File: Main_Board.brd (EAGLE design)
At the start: 160.3 x 95.4 mm, 227 parts, among them J1 SERVO, J2 5.5x2.1mm Barrel, J3 9.7uH, J4 BATTERY, J5 SPEAKER, J6 SDIO-SDCARD, J7 header, P1 MOTOR_HEADER, P2 MOTOR_HEADER, P3 JTAG, Q1 SI9933CDY-PFET, Q2 CSD17308Q3, Q3 CSD17308Q3, Q4 CSD17308Q3, Q5 CSD17308Q3, Q6 CSD17308Q3, Q7 CSD17308Q3, Q8 CSD17308Q3, U1 LMS8117, U10 IMU, U11 LTC3122-MSOP, U12 CBAT54S-SOT23-3, U13 BQ2947, U14 TPA2005D1DGN, U15 BQ40Z60, U2 5V_BUCK_REG, U3 BTM7752G, U4 BTM7752G, U5 SN74LV4T125, U6 SN74LV4T125, U7 STM32F405RGT6, U8 RN4020RN4020, U9 BQ51013B-20VQFN

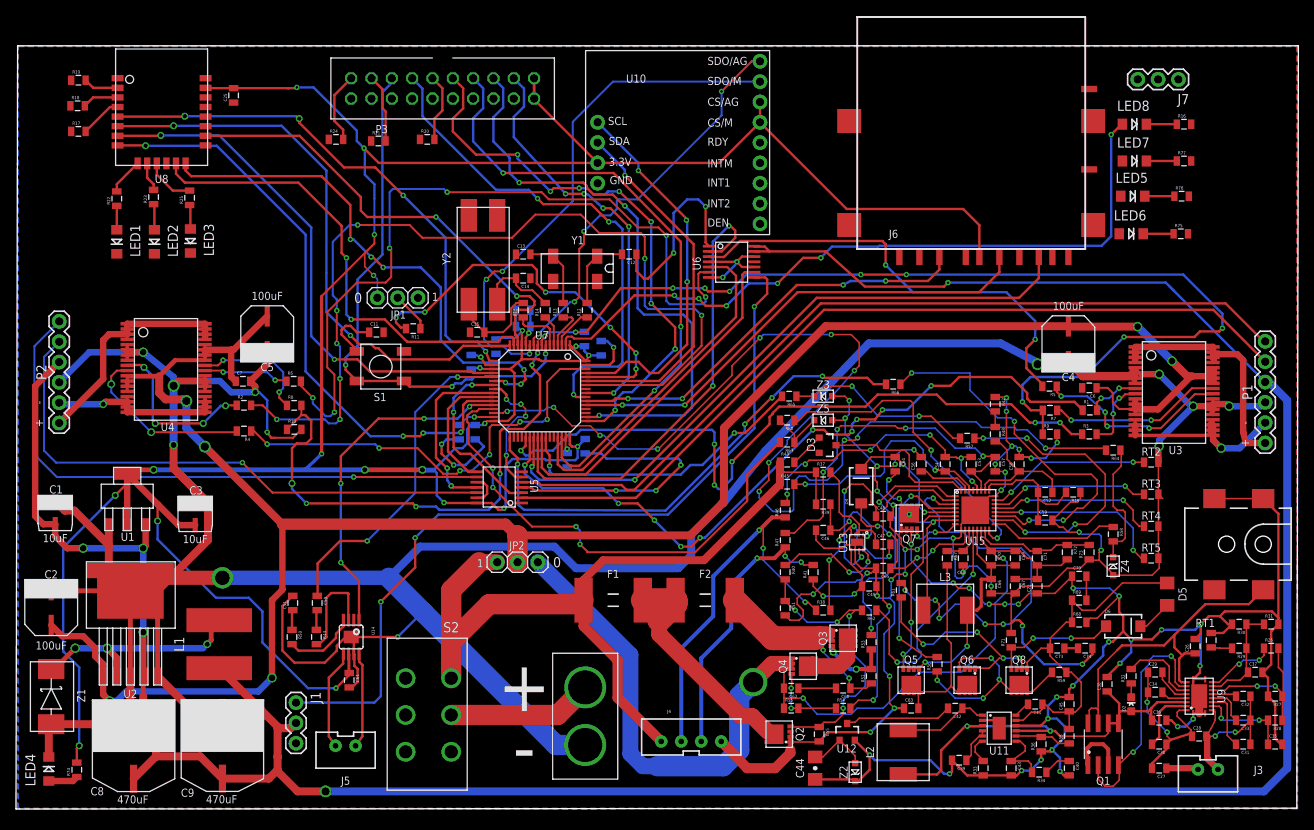
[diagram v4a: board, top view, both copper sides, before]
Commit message: routed LED, added standoffs, and refined routes
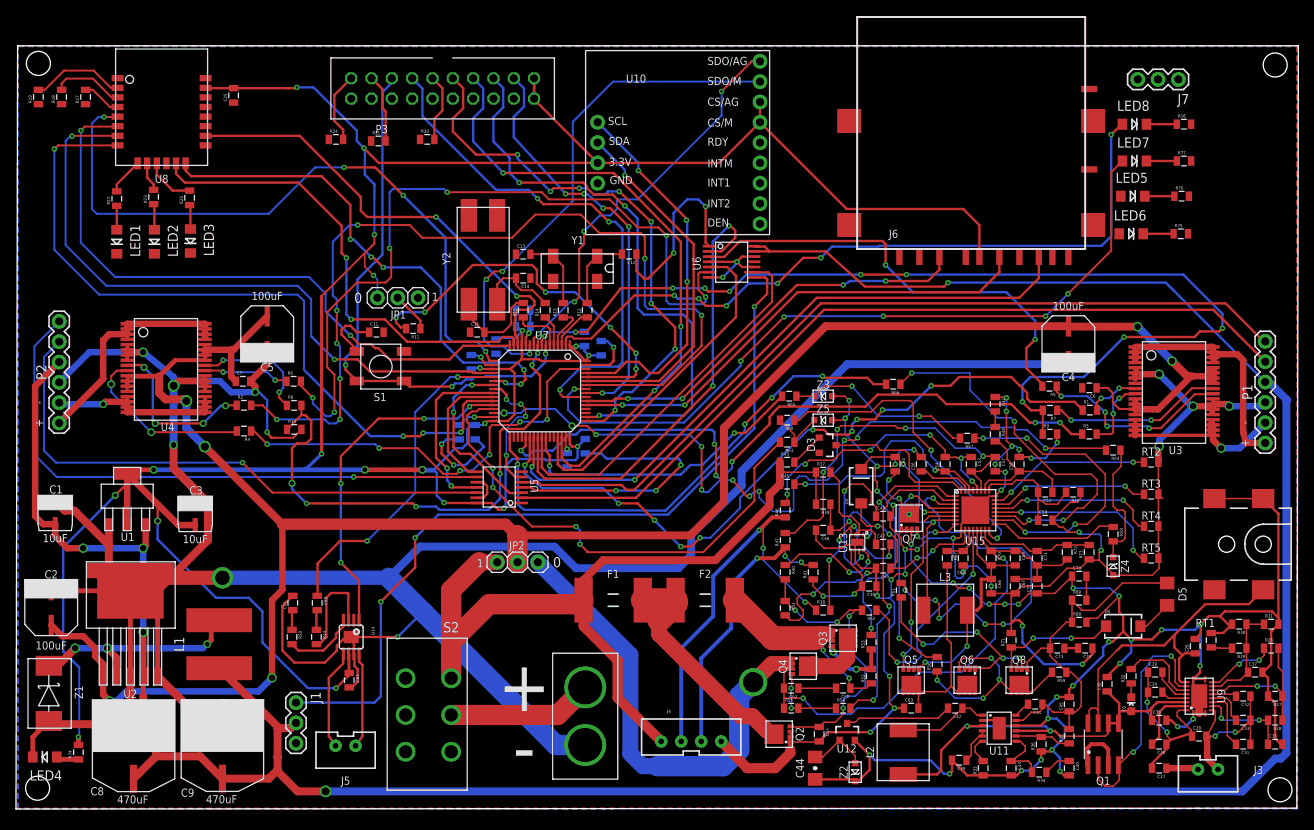
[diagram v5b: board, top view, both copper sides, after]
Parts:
- moved R19 5.42 mm to (2.80, 89.0), turned to 90 degrees
- moved R17 4.39 mm to (8.70, 89.0), turned to 90 degrees
- moved R18 2.28 mm to (5.70, 89.0), turned to 90 degrees
- moved R74 2.21 mm to (7.80, 7.10)
- moved LED4 1.58 mm to (3.60, 6.50), turned to 180 degrees
- moved Z1 0.50 mm to (4.10, 11.0)
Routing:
- net N$133: track 0.00 -> 94.0 mm, vias 0 -> 6
- net CHRG_I2C_SDA: track 134.2 -> 98.2 mm, vias 12 -> 11
- net GND: track 797.4 -> 778.9 mm
- net BLU_CMD: track 75.7 -> 93.9 mm
- net BLU_TX: track 67.5 -> 84.7 mm
- net BLUE_WAKE_SW: track 67.3 -> 82.6 mm
- net BLU_RX: track 72.2 -> 80.5 mm
- net N$7: track 4.39 -> 11.8 mm
- net N$48: track 4.53 -> 9.02 mm
- net SERVO_PWM_3.3: track 44.4 -> 48.8 mm
- net MC1_IN2: track 89.4 -> 86.6 mm
- net JTDO: track 63.7 -> 66.0 mm
- net 3.3V: track 409.8 -> 407.6 mm
- net 5V: track 358.4 -> 357.3 mm
- net N$42: track 3.71 -> 2.82 mm
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
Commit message: Updated cap pads to be slightly larager for easy soldering
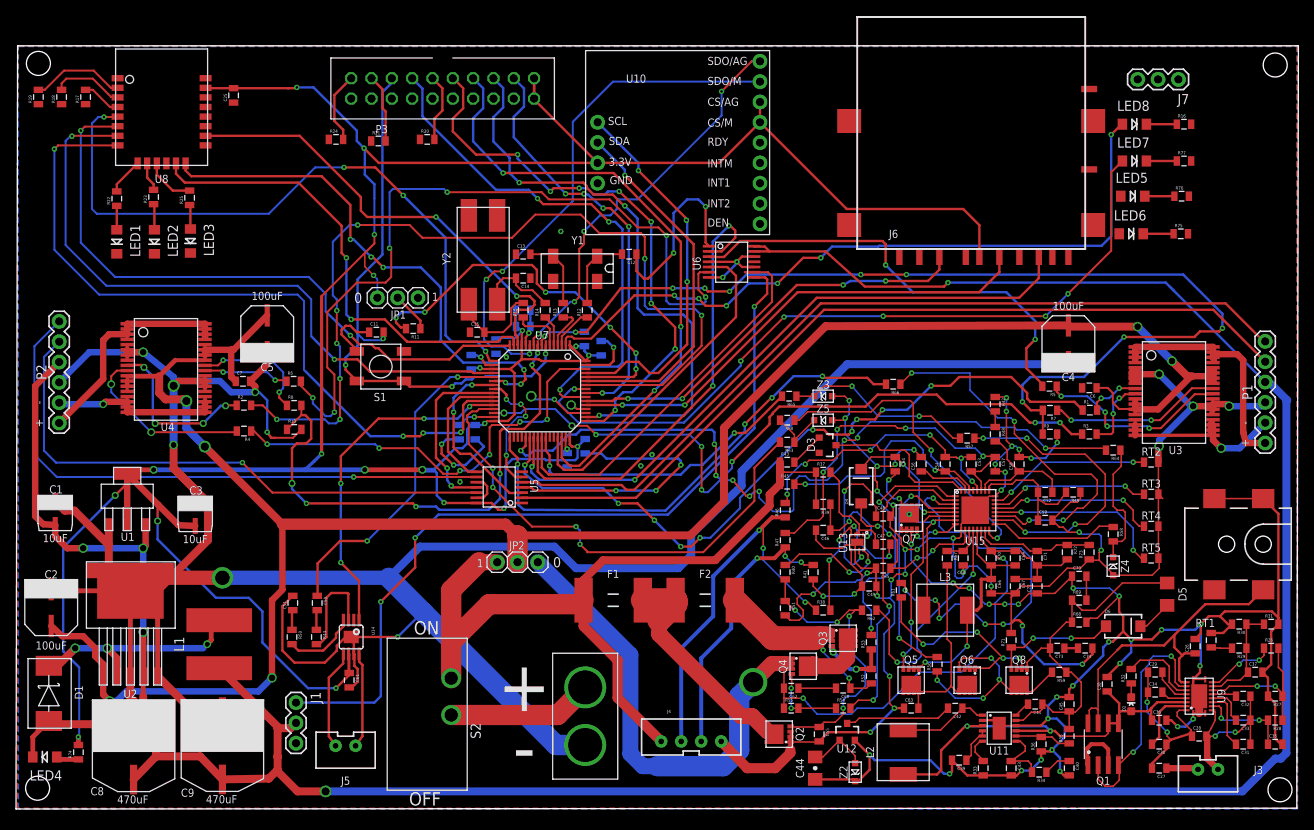
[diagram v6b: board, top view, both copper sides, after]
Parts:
- J3: value 9.7uH -> (none)
- R22, R23, R25, R74: value 10K -> 1K
- Y1: value (none) -> 32.768KHz
- Y2: value (none) -> 25MHz
- renumbered Z1 to D1
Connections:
- net !NRST: now also C11.2
- net GND: no longer C11.2
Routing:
- net N$45: track 0.00 -> 7.79 mm, vias 0 -> 2
- net !NRST: track 68.1 -> 72.6 mm, vias 3 -> 4
- net N$47: track 0.00 -> 2.13 mm, vias 0 -> 1
- net N$133: track 94.0 -> 95.3 mm
- net GND: track 778.9 -> 778.6 mm, vias 57 -> 61

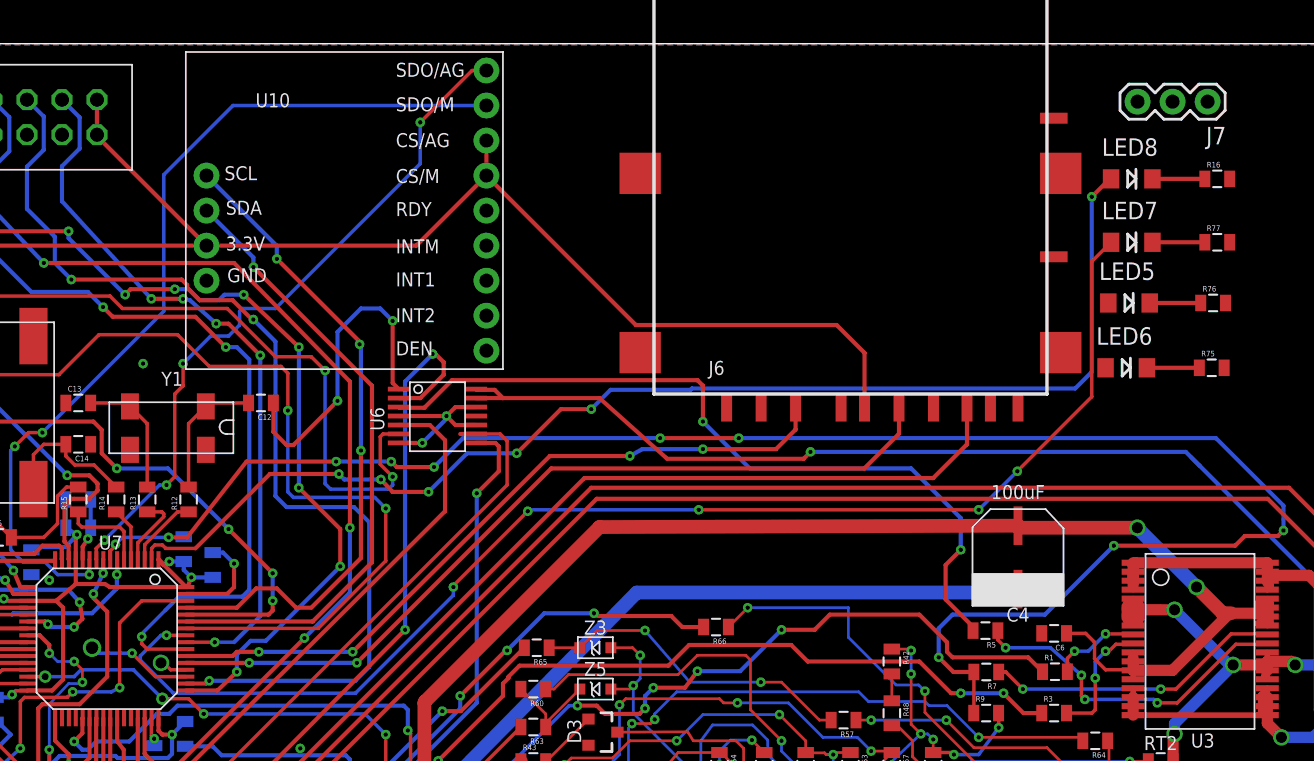
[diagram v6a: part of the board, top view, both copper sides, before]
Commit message: Removed LEDs and 3 pin header since it wasn't worth trying to route
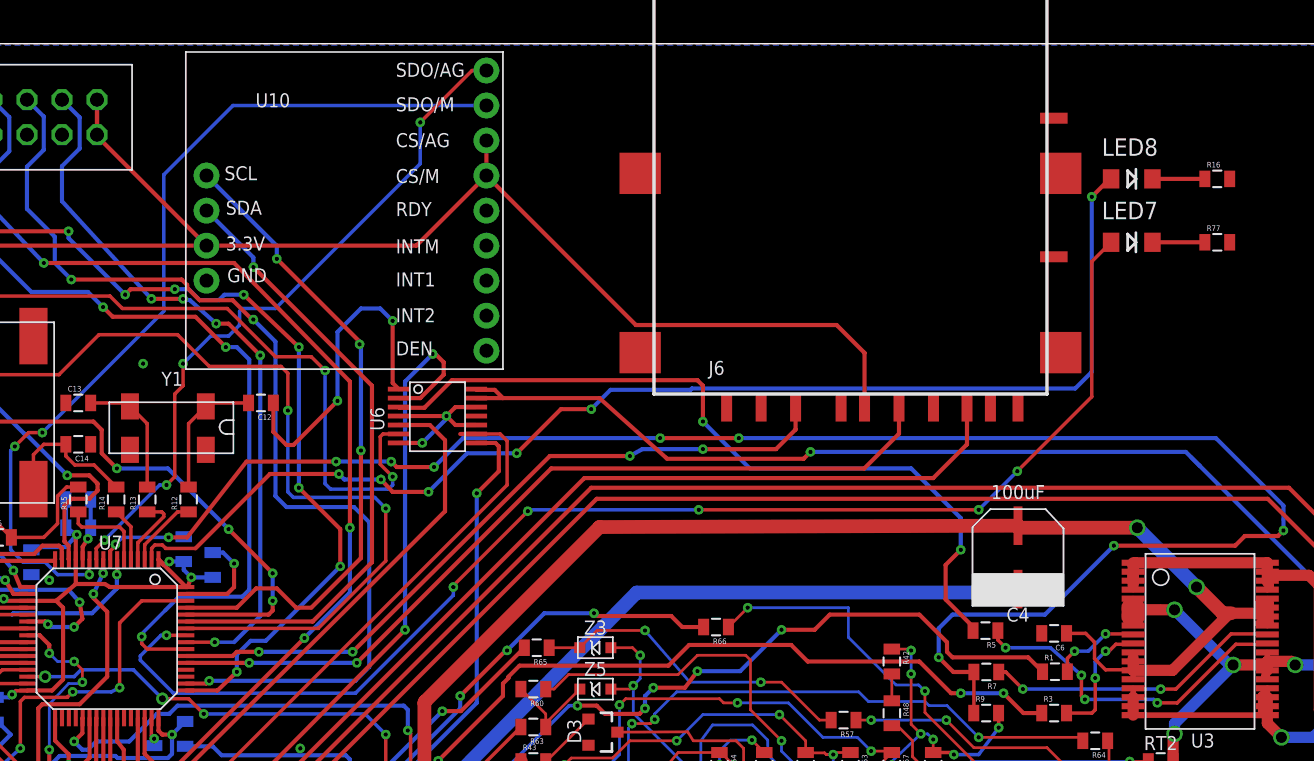
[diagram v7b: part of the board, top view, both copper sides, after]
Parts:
- removed J7: header, SparkFun-Connectors:1X03
- removed LED5, LED6: (no value), LilyPad-Wearables:LED-1206
- removed R75, R76: 100, SparkFun-Resistors:0805
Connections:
- removed net N$131: LED6.C, R75.1
- removed net N$132: LED5.C, R76.1
- removed net N$27: J7.1, U7.P$36
- removed net N$43: J7.2, U7.P$35
- removed net N$44: J7.3, U7.P$34
- removed net N$45: LED6.A, U7.P$51
- removed net N$47: LED5.A, U7.P$52
- net GND: no longer R75.2, R76.2
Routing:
- net N$45: track 7.79 -> 0.00 mm, vias 2 -> 0
- net N$131: track 3.80 -> 0.00 mm
- net N$132: track 3.70 -> 0.00 mm
- net N$47: track 2.13 -> 0.00 mm, vias 1 -> 0
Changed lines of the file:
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@@
 <layer number="22" name="bPlace" color="7" fill="1" visible="yes" active="yes"/>
 <layer number="23" name="tOrigins" color="15" fill="1" visible="yes" active="yes"/>
-<layer number="24" name="bOrigins" color="15" fill="1" visible="no" active="yes"/>
-<layer number="25" name="tNames" color="7" fill="1" visible="no" active="yes"/>
-<layer number="26" name="bNames" color="7" fill="1" visible="no" active="yes"/>
-<layer number="27" name="tValues" color="7" fill="1" visible="no" active="yes"/>
-<layer number="28" name="bValues" color="7" fill="1" visible="no" active="yes"/>
+<layer number="24" name="bOrigins" color="15" fill="1" visible="yes" active="yes"/>
+<layer number="25" name="tNames" color="7" fill="1" visible="yes" active="yes"/>
+<layer number="26" name="bNames" color="7" fill="1" visible="yes" active="yes"/>
+<layer number="27" name="tValues" color="7" fill="1" visible="yes" active="yes"/>
+<layer number="28" name="bValues" color="7" fill="1" visible="yes" active="yes"/>
 <layer number="29" name="tStop" color="7" fill="3" visible="no" active="yes"/>
 <layer number="30" name="bStop" color="7" fill="6" visible="no" active="yes"/>
@@
 <layer number="43" name="vRestrict" color="2" fill="10" visible="no" active="yes"/>
 <layer number="44" name="Drills" color="7" fill="1" visible="no" active="yes"/>
-<layer number="45" name="Holes" color="7" fill="1" visible="no" active="yes"/>
+<layer number="45" name="Holes" color="7" fill="1" visible="yes" active="yes"/>
 <layer number="46" name="Milling" color="3" fill="1" visible="no" active="yes"/>
 <layer number="47" name="Measures" color="7" fill="1" visible="no" active="yes"/>
@@
 <element name="R74" library="SparkFun-Passives" package="0805" value="1K" x="7.8" y="7.1" rot="R90"/>
 <element name="LED4" library="LilyPad-Wearables" package="LED-1206" value="" x="3.6" y="6.5" rot="R180"/>
-<element name="J7" library="SparkFun-Connectors" package="1X03" value="header" x="145.3" y="91.2" rot="R180"/>
-<element name="LED5" library="LilyPad-Wearables" package="LED-1206" value="" x="139.6" y="76.6"/>
-<element name="LED6" library="LilyPad-Wearables" package="LED-1206" value="" x="139.4" y="71.9"/>
-<element name="R75" library="SparkFun-Resistors" package="0805" value="100" x="145.6" y="71.9"/>
-<element name="R76" library="SparkFun-Resistors" package="0805" value="100" x="145.7" y="76.6"/>
 <element name="R77" library="SparkFun-Resistors" package="0805" value="100" x="146" y="81"/>
 <element name="LED7" library="LilyPad-Wearables" package="LED-1206" value="" x="139.8" y="81"/>
@@
 <contactref element="U14" pad="7"/>
 <contactref element="R77" pad="2"/>
-<contactref element="R75" pad="2"/>
-<contactref element="R76" pad="2"/>
 <wire x1="14.3" y1="27.275" x2="4.4" y2="27.275" width="0.6096" layer="1"/>
 <wire x1="4.4" y1="27.275" x2="4.4" y2="27.48" width="0.6096" layer="1"/>
@@
 <wire x1="5.4" y1="6.2" x2="7.8" y2="6.2" width="0.6096" layer="1"/>
 </signal>
-<signal name="N$27">
-<contactref element="U7" pad="P$36"/>
-<contactref element="J7" pad="1"/>
-<wire x1="63.22" y1="46.5" x2="145.3" y2="91.2" width="0" layer="19" extent="1-1"/>
-</signal>
-<signal name="N$43">
-<contactref element="U7" pad="P$35"/>
-<contactref element="J7" pad="2"/>
-<wire x1="62.72" y1="46.5" x2="142.76" y2="91.2" width="0" layer="19" extent="1-1"/>
-</signal>
-<signal name="N$44">
-<contactref element="U7" pad="P$34"/>
-<contactref element="J7" pad="3"/>
-<wire x1="62.22" y1="46.5" x2="140.22" y2="91.2" width="0" layer="19" extent="1-1"/>
-</signal>
-<signal name="N$45">
-<contactref element="U7" pad="P$51"/>
-<contactref element="LED6" pad="A"/>
-<wire x1="71.22" y1="49.5" x2="69" y2="49.5" width="0.254" layer="1"/>
-<wire x1="69" y1="49.5" x2="67.3" y2="51.2" width="0.254" layer="1"/>
-<via x="67.3" y="51.2" extent="1-16" drill="0.3"/>
-<wire x1="67.3" y1="51.2" x2="64.8" y2="51.2" width="0.254" layer="16"/>
-<wire x1="64.8" y1="51.2" x2="64.4" y2="51.6" width="0.254" layer="16"/>
-<via x="64.4" y="51.6" extent="1-16" drill="0.9"/>
-<wire x1="64.4" y1="51.6" x2="64.3" y2="51.6" width="0.254" layer="1"/>
-<wire x1="64.3" y1="51.6" x2="137.9" y2="71.9" width="0" layer="19" extent="1-16"/>
-</signal>
-<signal name="N$47">
-<contactref element="LED5" pad="A"/>
-<contactref element="U7" pad="P$52"/>
-<wire x1="71.22" y1="50" x2="70.1" y2="50" width="0.254" layer="1"/>
-<wire x1="70.1" y1="50" x2="69.6" y2="50.5" width="0.254" layer="1"/>
-<wire x1="69.6" y1="50.5" x2="69.4" y2="50.5" width="0.254" layer="1"/>
-<via x="69.4" y="50.5" extent="1-16" drill="0.8"/>
-<wire x1="69.4" y1="50.5" x2="69.3" y2="50.5" width="0.254" layer="16"/>
-<wire x1="69.3" y1="50.5" x2="138.1" y2="76.6" width="0" layer="19" extent="1-16"/>
-</signal>
-<signal name="N$131">
-<contactref element="LED6" pad="C"/>
-<contactref element="R75" pad="1"/>
-<wire x1="140.9" y1="71.9" x2="144.7" y2="71.9" width="0.3048" layer="1"/>
-</signal>
-<signal name="N$132">
-<contactref element="LED5" pad="C"/>
-<contactref element="R76" pad="1"/>
-<wire x1="141.1" y1="76.6" x2="144.8" y2="76.6" width="0.3048" layer="1"/>
-</signal>
 <signal name="N$133">
 <contactref element="U7" pad="P$57"/>
@@
 <wire x1="71.22" y1="52.5" x2="69.8" y2="52.5" width="0.254" layer="1"/>
 <via x="69.8" y="52.5" extent="1-16" drill="0.3"/>
-<wire x1="69.8" y1="52.5" x2="69" y2="51.7" width="0" layer="19" extent="1-16"/>
 <wire x1="70.3" y1="48.3" x2="83.5" y2="48.3" width="0.254" layer="16"/>
 <wire x1="83.5" y1="48.3" x2="90.6" y2="55.4" width="0.254" layer="16"/>
